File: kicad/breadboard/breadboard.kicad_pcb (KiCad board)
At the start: 2 copper layers, 99.8 x 100.1 mm, 111 parts, among them J1 1, J10 2, J100 Conn_01x02, J101 Conn_01x02, J102 Conn_01x02, J103 Conn_01x02, J104 Conn_01x40, J105 Conn_01x40, J11 3, J12 3, J13 1, J14 1, J15 2, J16 2, J17 3, J18 3, J19 1, J2 1, J20 1, J21 2, J22 2, J23 3, J24 3, J25 1, J26 1, J27 2, J28 2, J29 3, J3 2, J30 3, J31 1, J32 1, J33 2, J34 2, J35 3, J36 3, J37 1, J38 1, J39 2, J4 2, J40 2, J41 3, J42 3, J43 1, J44 1, J45 2, J46 2, J47 3, J48 3, J49 Barrel_Jack, J5 3, J50 Conn_01x02, J51 Conn_01x02, J52 Conn_01x02, J53 Conn_01x02, J54 Conn_01x02, J55 Conn_01x02, J56 Conn_01x02, J57 Conn_01x02, J58 Conn_01x02, J59 Conn_01x02, J6 3, J60 Conn_01x02, J61 Conn_01x02, J62 Conn_01x02, J63 Conn_01x02, J64 Conn_01x40, J65 Conn_01x40, J66 Conn_01x02, J67 Conn_01x02, J68 Conn_01x02, J69 Conn_01x02, J7 1, J70 Conn_01x02, J71 Conn_01x02, J72 Conn_01x02, J73 Conn_01x02, J74 Conn_01x02, J75 Conn_01x02, J76 Conn_01x02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

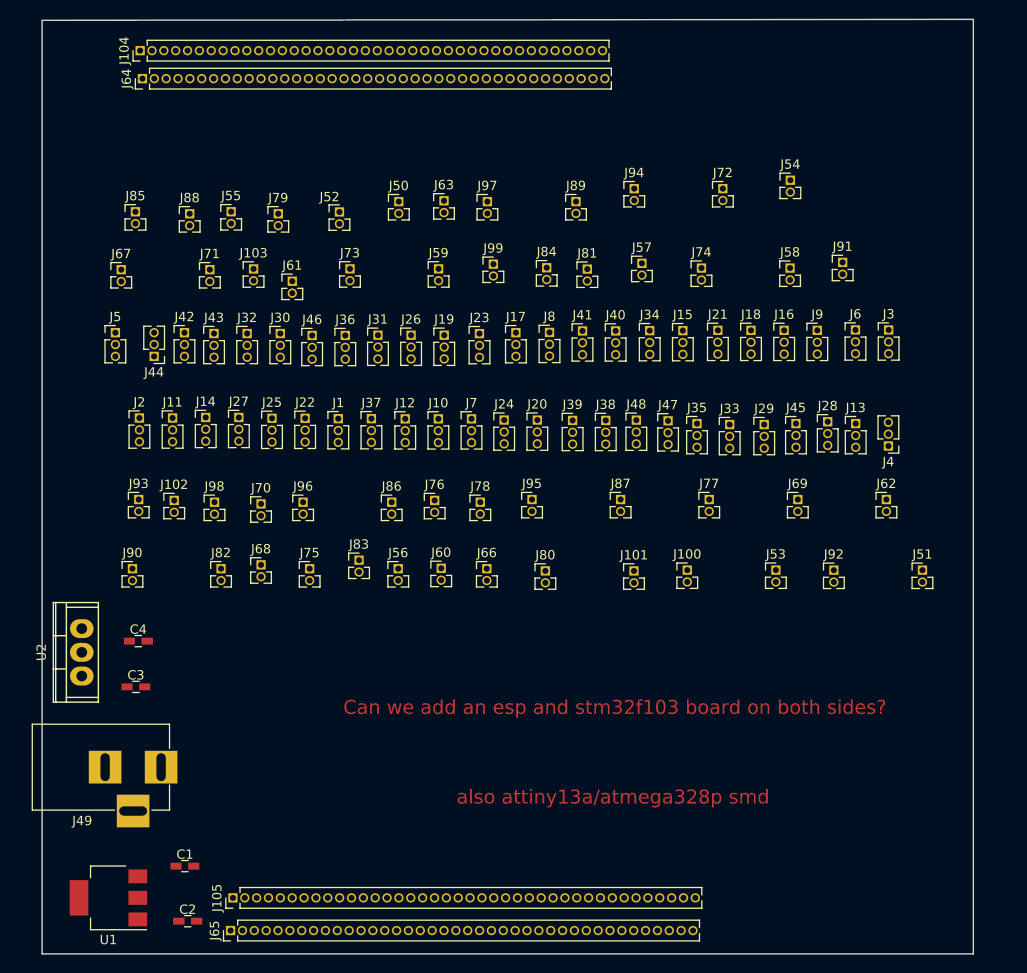
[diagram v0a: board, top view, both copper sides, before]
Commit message: breadboard: Add esp12e into board
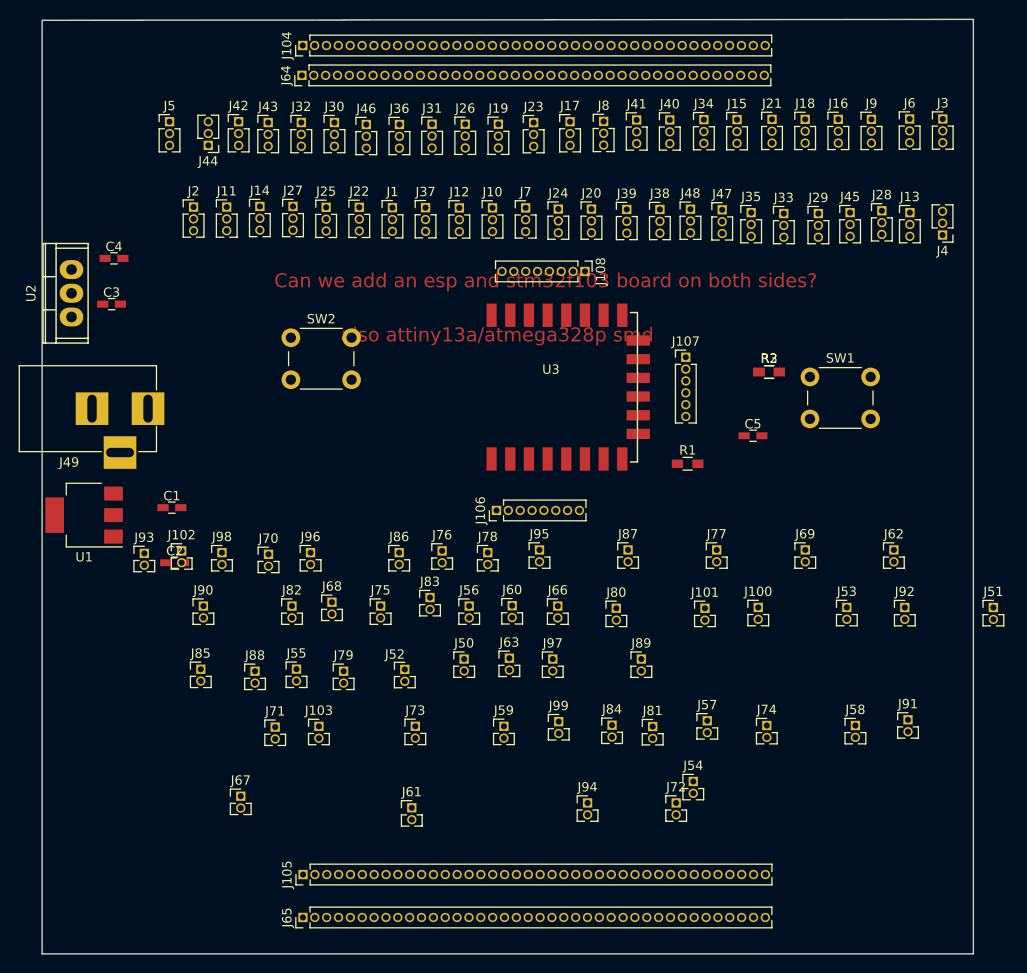
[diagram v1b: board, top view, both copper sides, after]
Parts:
- added C5: C, Capacitors_SMD:C_0603_HandSoldering, F.Cu at (161.4, 77.0)
- added J106: Conn_01x08, Pin_Headers:Pin_Header_Straight_1x08_Pitch1.27mm, F.Cu at (133.9, 85.0)
- added J107: Conn_01x06, Pin_Headers:Pin_Header_Straight_1x06_Pitch1.27mm, F.Cu at (154.2, 68.6)
- added J108: Conn_01x08, Pin_Headers:Pin_Header_Straight_1x08_Pitch1.27mm, F.Cu at (143.4, 59.4)
- added R1: 10k, Resistors_SMD:R_0603_HandSoldering, F.Cu at (154.4, 80.0)
- added R2, R3: 10k, Resistors_SMD:R_0603_HandSoldering, F.Cu at (163.1, 70.2)
- added SW1: SWITCH, Buttons_Switches_THT:SW_PUSH_6mm, F.Cu at (167.5, 70.7)
- added SW2: SWITCH, Buttons_Switches_THT:SW_PUSH_6mm, F.Cu at (111.9, 66.5)
- added U3: ESP-12E, ESP8266:ESP-12E_SMD, F.Cu at (133.4, 78.8)
- moved J72 66.0 mm to (153.2, 116.3)
- moved J94 66.0 mm to (143.7, 116.3)
- moved J54 65.2 mm to (155.0, 114.0)
- moved J67 57.8 mm to (106.5, 115.6)
- moved J61 57.8 mm to (124.8, 116.8)
- moved J58 49.5 mm to (172.4, 108.0)
- moved J59 49.5 mm to (134.7, 108.1)
- moved J73 49.5 mm to (125.2, 108.1)
- moved J74 49.5 mm to (162.9, 108.0)
- moved J81 49.5 mm to (150.7, 108.2)
- moved J85 49.5 mm to (102.2, 102.0)
- moved J91 49.5 mm to (178.0, 107.4)
- moved J99 49.5 mm to (140.6, 107.6)
- moved J50 49.5 mm to (130.5, 100.9)
- moved J52 49.5 mm to (124.1, 102.0)
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
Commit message: breadboard: esp12e - work is almost completed.
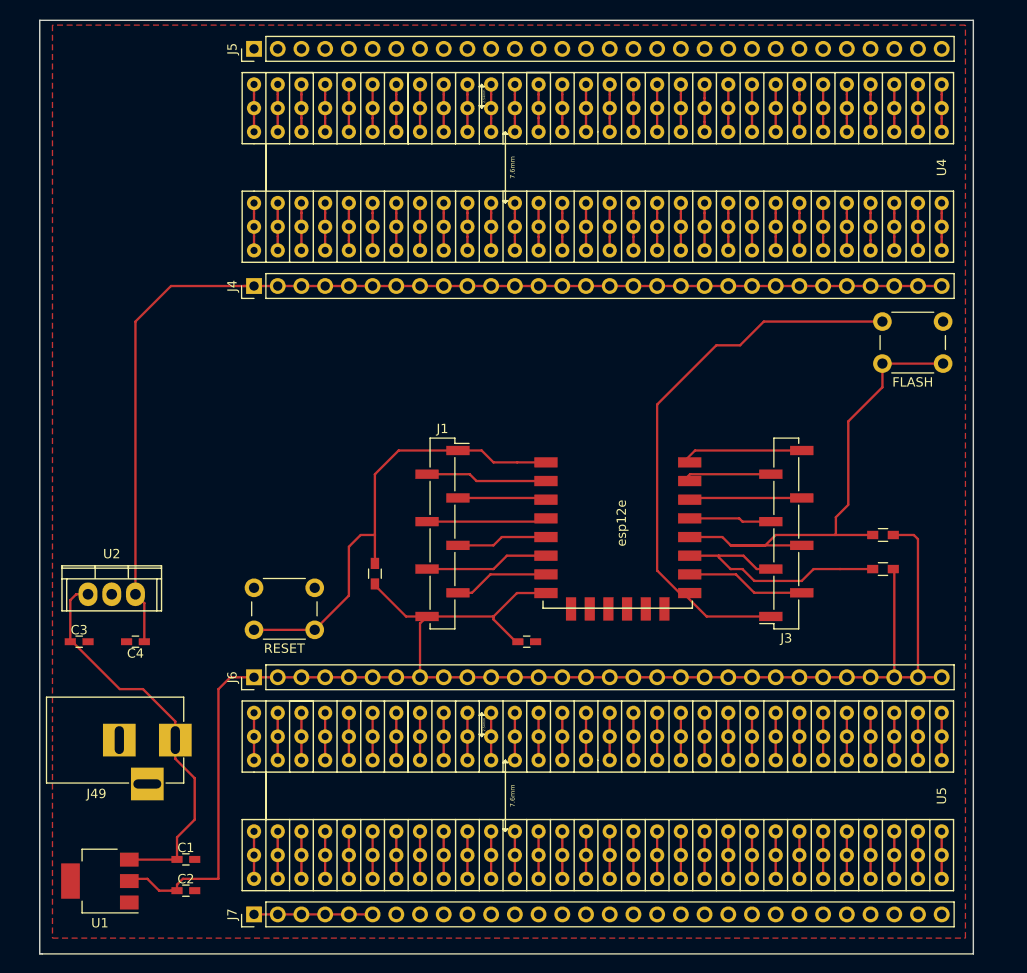
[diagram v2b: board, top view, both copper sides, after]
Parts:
- removed J10, J15, J16, J21, J22, J27, J28, J33, J34, J39, J40, J45, J46, J9: 2, Pin_Headers:Pin_Header_Straight_1x03_Pitch1.27mm
- removed J100, J101, J102, J103, J50, J51, J52, J53, J54, J55, J56, J57, J58, J59, J60, J61, J62, J63, J66, J67, J68, J69, J70, J71, J72, J73, J74, J75, J76, J77, J78, J79, J80, J81, J82, J83, J84, J85, J86, J87, J88, J89, J90, J91, J92, J93, J94, J95, J96, J97, J98, J99: Conn_01x02, Pin_Headers:Pin_Header_Straight_1x02_Pitch1.27mm
- removed J104, J105, J64, J65: Conn_01x40, Pin_Headers:Pin_Header_Straight_1x40_Pitch1.27mm
- removed J106, J108: Conn_01x08, Pin_Headers:Pin_Header_Straight_1x08_Pitch1.27mm
- removed J107: Conn_01x06, Pin_Headers:Pin_Header_Straight_1x06_Pitch1.27mm
- removed J11, J12, J17, J18, J23, J24, J29, J30, J35, J36, J41, J42, J47, J48: 3, Pin_Headers:Pin_Header_Straight_1x03_Pitch1.27mm
- removed J13, J14, J19, J2, J20, J25, J26, J31, J32, J37, J38, J43, J44, J8: 1, Pin_Headers:Pin_Header_Straight_1x03_Pitch1.27mm
- added U4: bboard_3rows, breadboard:bboard_3rows_footprint, F.Cu at (144.8, 48.3)
- added U5: bboard_3rows, breadboard:bboard_3rows_footprint, F.Cu at (144.8, 115.6)
- J1: value 1 -> Conn_01x08; footprint Pin_Headers:Pin_Header_Straight_1x03_Pitch1.27mm -> Pin_Headers:Pin_Header_Straight_1x08_Pitch2.54mm_SMD_Pin1Right
- J3: value 2 -> Conn_01x08; footprint Pin_Headers:Pin_Header_Straight_1x03_Pitch1.27mm -> Pin_Headers:Pin_Header_Straight_1x08_Pitch2.54mm_SMD_Pin1Right
- J4: value 2 -> Conn_01x30; footprint Pin_Headers:Pin_Header_Straight_1x03_Pitch1.27mm -> Pin_Headers:Pin_Header_Straight_1x30_Pitch2.54mm
- J5, J6: value 3 -> Conn_01x30; footprint Pin_Headers:Pin_Header_Straight_1x03_Pitch1.27mm -> Pin_Headers:Pin_Header_Straight_1x30_Pitch2.54mm
- J7: value 1 -> Conn_01x30; footprint Pin_Headers:Pin_Header_Straight_1x03_Pitch1.27mm -> Pin_Headers:Pin_Header_Straight_1x30_Pitch2.54mm
- RESET: renamed from SW1; value SWITCH -> RESET
- moved J6 92.2 mm to (108.0, 102.9), turned to 90 degrees
- moved J7 81.1 mm to (108.0, 128.3), turned to 90 degrees
- moved J4 74.0 mm to (108.0, 61.0), turned to 90 degrees
- moved FLASH 69.9 mm to (181.8, 69.3), turned to 180 degrees
- moved RESET 59.6 mm to (114.5, 97.8), turned to 180 degrees
- moved J3 47.5 mm to (165.0, 87.5), turned to 180 degrees
- moved C4 41.1 mm to (95.2, 99.1), turned to 180 degrees
- moved U1 39.2 mm to (91.4, 124.7)
- moved C1 37.7 mm to (100.7, 122.4)
- moved C3 36.3 mm to (89.2, 99.1)
- moved J49 35.6 mm to (99.5, 109.6)
- moved R1 35.5 mm to (120.9, 91.8), turned to 270 degrees
- moved J1 35.3 mm to (128.1, 87.5)
- moved C2 35.2 mm to (100.7, 125.7)
- moved C5 32.8 mm to (137.2, 99.1), turned to 180 degrees
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- renumbered SW2 to FLASH, U3 to esp12e
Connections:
- C2 pad 1: /V3.3v -> V3.3v
- C5 pad 2: /V3.3v -> V3.3v
- FLASH pad 1: Net-(J108-Pad4) -> Net-(J3-Pad4)
- J1 pad 2: Net-(J1-Pad1) -> Net-(J1-Pad2)
- J1 pad 3: Net-(J1-Pad1) -> Net-(J1-Pad3)
- J3 pad 1: Net-(J3-Pad1) -> GND
- J3 pad 2: Net-(J3-Pad1) -> Net-(J3-Pad2)
- J3 pad 3: Net-(J3-Pad1) -> Net-(J3-Pad3)
- J4 pad 1: Net-(J4-Pad1) -> /V5v
- J4 pad 2: Net-(J4-Pad1) -> /V5v
- J4 pad 3: Net-(J4-Pad1) -> /V5v
- J5 pad 1: Net-(J5-Pad1) -> GND
- J5 pad 2: Net-(J5-Pad1) -> GND
- J5 pad 3: Net-(J5-Pad1) -> GND
- J6 pad 1: Net-(J6-Pad1) -> V3.3v
- J6 pad 2: Net-(J6-Pad1) -> V3.3v
- J6 pad 3: Net-(J6-Pad1) -> V3.3v
- J7 pad 1: Net-(J7-Pad1) -> GND
- J7 pad 2: Net-(J7-Pad1) -> GND
- J7 pad 3: Net-(J7-Pad1) -> GND
- R1 pad 1: Net-(J106-Pad1) -> Net-(J1-Pad1)
- R1 pad 2: /V3.3v -> V3.3v
- R2 pad 1: /V3.3v -> V3.3v
- R2 pad 2: Net-(J108-Pad3) -> Net-(J3-Pad3)
- R3 pad 1: Net-(J108-Pad4) -> Net-(J3-Pad4)
- R3 pad 2: /V3.3v -> V3.3v
- RESET pad 1: Net-(J106-Pad1) -> Net-(J1-Pad1)
- U1 pad 2: /V3.3v -> V3.3v
- esp12e pad 1: Net-(J106-Pad1) -> Net-(J1-Pad1)
- esp12e pad 10: Net-(J108-Pad2) -> Net-(J3-Pad2)
- esp12e pad 11: Net-(J108-Pad3) -> Net-(J3-Pad3)
- esp12e pad 12: Net-(J108-Pad4) -> Net-(J3-Pad4)
- esp12e pad 13: Net-(J108-Pad5) -> Net-(J3-Pad5)
- esp12e pad 14: Net-(J108-Pad6) -> Net-(J3-Pad6)
- esp12e pad 15: Net-(J108-Pad7) -> Net-(J3-Pad7)
- esp12e pad 16: Net-(J108-Pad8) -> Net-(J3-Pad8)
- esp12e pad 2: Net-(J106-Pad2) -> Net-(J1-Pad2)
- esp12e pad 3: Net-(J106-Pad3) -> Net-(J1-Pad3)
- esp12e pad 4: Net-(J106-Pad4) -> Net-(J1-Pad4)
- esp12e pad 5: Net-(J106-Pad5) -> Net-(J1-Pad5)
- esp12e pad 6: Net-(J106-Pad6) -> Net-(J1-Pad6)
- esp12e pad 7: Net-(J106-Pad7) -> Net-(J1-Pad7)
- esp12e pad 8: /V3.3v -> V3.3v
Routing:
- net V3.3v: track 0.00 -> 171.9 mm
- net /V5v: track 0.00 -> 124.0 mm
- net GND: track 0.00 -> 72.5 mm
- net Net-(J3-Pad4): track 0.00 -> 55.7 mm
- net Net-(J1-Pad1): track 0.00 -> 50.4 mm
- net VCC: track 0.00 -> 42.9 mm
- net Net-(J3-Pad3): track 0.00 -> 28.2 mm
- net Net-(J1-Pad6): track 0.00 -> 14.0 mm
- net Net-(J1-Pad2): track 0.00 -> 13.7 mm
- net Net-(J1-Pad4): track 0.00 -> 13.6 mm
- net Net-(J3-Pad2): track 0.00 -> 13.5 mm
- net Net-(J3-Pad8): track 0.00 -> 13.2 mm
- net Net-(J3-Pad6): track 0.00 -> 12.8 mm
- net Net-(J1-Pad7): track 0.00 -> 10.9 mm
- net Net-(J1-Pad5): track 0.00 -> 10.5 mm
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- added copper zone on F.Cu, net GND
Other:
- board size 99.8 x 100.1 mm -> 100 x 100 mm
- board text removed: "Can we add an esp and stm32f103 board on both sides?"
- board text removed: "also attiny13a/atmega328p smd"

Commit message: fix sch
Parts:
- removed FLASH: SWITCH, Buttons_Switches_THT:SW_PUSH_6mm
- removed RESET: RESET, Buttons_Switches_THT:SW_PUSH_6mm
- removed esp12e: ESP-12E, ESP8266:ESP-12E_SMD
- added SW1: SWITCH, Buttons_Switches_THT:SW_PUSH_6mm, F.Cu at (108.4, 93.7)
- added SW2: SWITCH, Buttons_Switches_THT:SW_PUSH_6mm, F.Cu at (175.3, 64.8)
- added U3: ESP-12E, ESP8266:ESP-12E_SMD, F.Cu at (139.8, 79.8)
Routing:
- net GND: track 72.5 -> 79.8 mm
- net Net-(J1-Pad1): track 50.4 -> 43.9 mm
- net Net-(J3-Pad4): track 55.7 -> 61.8 mm
